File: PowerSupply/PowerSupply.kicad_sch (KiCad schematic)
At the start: 9 parts, among them J1 POWER, J2 CONTROL, J3 LASER, U0 AL8861Y-13

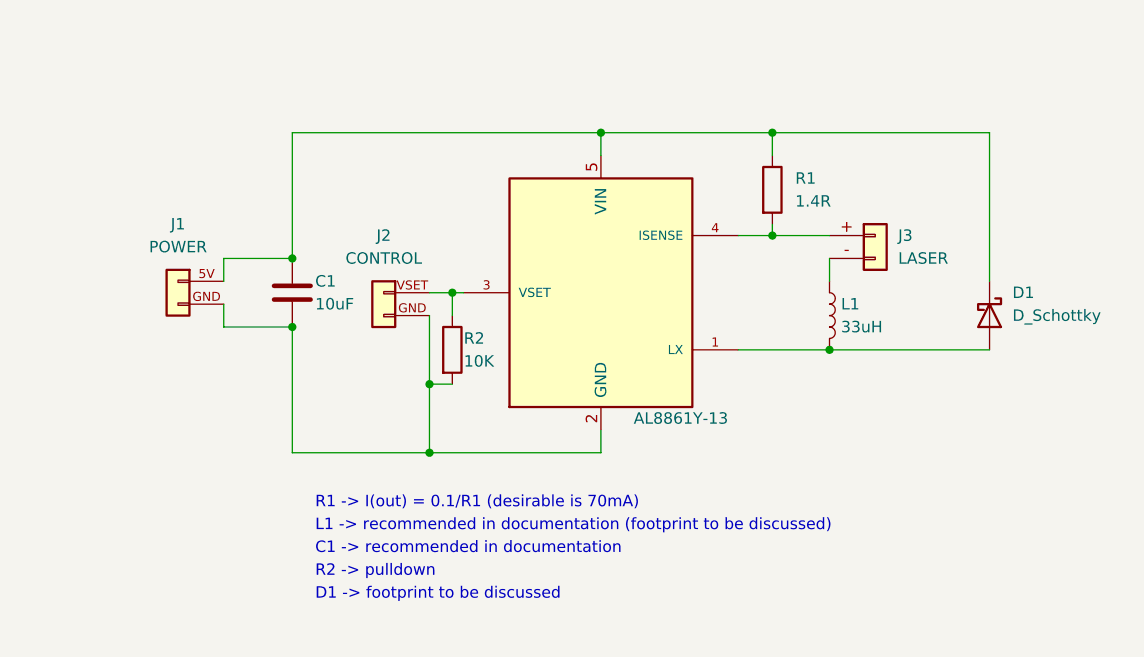
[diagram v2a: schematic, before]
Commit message: Add footprints
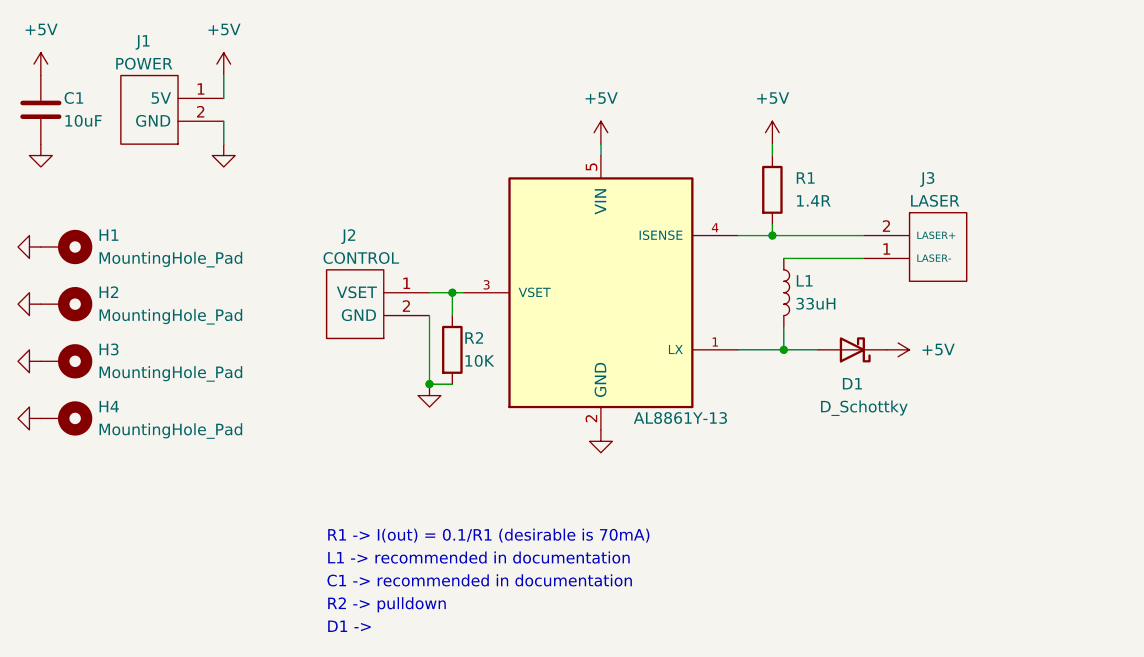
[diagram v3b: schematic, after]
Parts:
- removed J1: POWER, Connector_PinHeader_2.54mm:PinHeader_1x02_P2.54mm_Vertical, symbol Connector_Generic:Conn_01x02
- removed J2: CONTROL, Connector_PinHeader_2.54mm:PinHeader_1x02_P2.54mm_Vertical, symbol Connector_Generic:Conn_01x02
- removed J3: LASER, Connector_PinHeader_2.54mm:PinHeader_1x02_P2.54mm_Vertical, symbol Connector_Generic:Conn_01x02
- added H1, H2, H3, H4: MountingHole_Pad, MountingHole:MountingHole_3.2mm_M3_Pad, symbol Mechanical:MountingHole_Pad
- added J1: POWER, Connector_Molex:Molex_Nano-Fit_105313-xx02_1x02_P2.50mm_Horizontal, symbol Mouser:105313-1102
- added J2: CONTROL, Connector_Molex:Molex_Nano-Fit_105313-xx02_1x02_P2.50mm_Horizontal, symbol Mouser:105313-1102
- added J3: LASER, Connector_Molex:Molex_Nano-Fit_105313-xx02_1x02_P2.50mm_Horizontal, symbol Mouser:105313-1102
- C1: Height (none) -> 1.6; Manufacturer_Name (none) -> Kyocera AVX; Manufacturer_Part_Number (none) -> NOSA106M006R0800; Mouser Part Number (none) -> 581-NOSA106M006R0800; Mouser Price/Stock (none) -> https://cz.mouser.com/ProductDetail/Kyocera-AVX/NOSA106M006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
- D1: footprint Diode_SMD:D_1206_3216Metric_Pad1.42x1.75mm_HandSolder -> Diode_SMD:D_SOD-123F; Manufacturer_Name (none) -> Vishay; Manufacturer_Part_Number (none) -> SL02-GS08; Mouser Part Number (none) -> 78-SL02; Mouser Price/Stock (none) -> https://cz.mouser.com/ProductDetail/Vishay-Semiconductors/S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
- L1: footprint Inductor_SMD:L_1206_3216Metric_Pad1.42x1.75mm_HandSolder -> Custom:4800S; Height (none) -> 6; Manufacturer_Name (none) -> Murata; Manufacturer_Part_Number (none) -> 48330SC; Mouser Part Number (none) -> 580-48330SC; Mouser Price/Stock (none) -> https://cz.mouser.com/ProductDetail/Murata-Power-Solutions/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
- R1: Height (none) -> 0.5; Manufacturer_Name (none) -> Vishay; Manufacturer_Part_Number (none) -> CRCW12061R40FKEAHP; Mouser Part Number (none) -> 71-CRCW12061R40FKEAH; Mouser Price/Stock (none) -> https://cz.mouser.com/ProductDetail/Vishay-Dale/CRCW12061R4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
- R2: Height (none) -> 0.64; Manufacturer_Name (none) -> Vishay; Manufacturer_Part_Number (none) -> CRMA1206AF10M0DKEF; Mouser Part Number (none) -> 71-CRMA1206AF10M0DKF; Mouser Price/Stock (none) -> https://cz.mouser.com/ProductDetail/Vishay/CRMA1206AF10M0DK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
- U0: MANUFACTURER DIODES INCORPORATED -> (none); Manufacturer_Name (none) -> Diodes Incorporated; PARTREV 3-2 -> (none); STANDARD Manufacturer Recommendations -> (none)
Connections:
- net at R1.2, U0.4 (ISENSE): now also J3.2 (LASER+)
- net at L1.1: now also J3.1 (LASER-)
- net +5V: now reaches C1.1, D1.1 (K), R1.1, U0.5 (VIN)
- net +5V: now also J1.1 (5V)
- net GND: now reaches C1.2, R2.2, U0.2 (GND)
- net GND: now also H1.1, H2.1, H3.1, H4.1, J1.2 (GND), J2.2 (GND)
- net at R2.1, U0.3 (VSET): now also J2.1 (VSET)
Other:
- note added: "D1 ->"
- note added: "L1 -> recommended in documentation"
- note removed: "D1 -> footprint to be discussed"
- note removed: "L1 -> recommended in documentation (footprint to be discussed)"
- moved on the sheet: L1

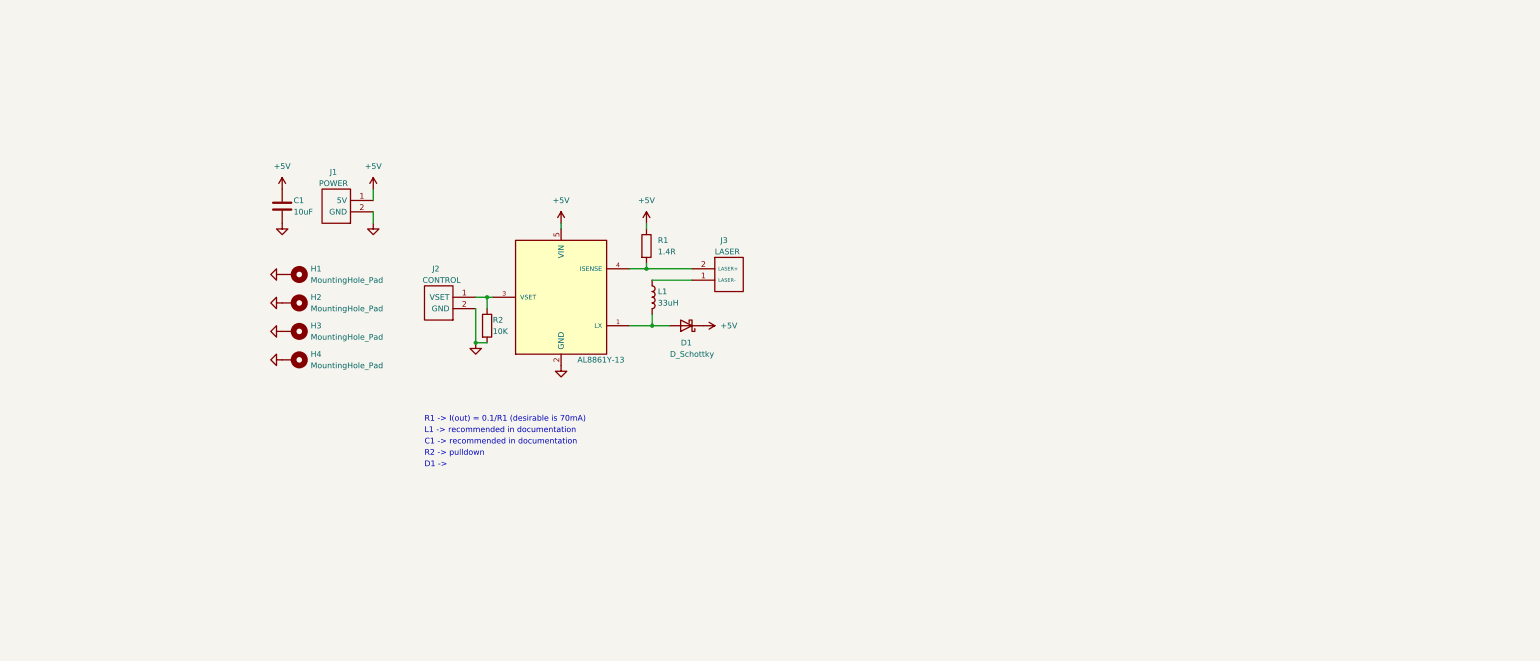
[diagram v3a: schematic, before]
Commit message: Review: 1st round - Schema & PCB - General modifications
All comments in design files, more on chat
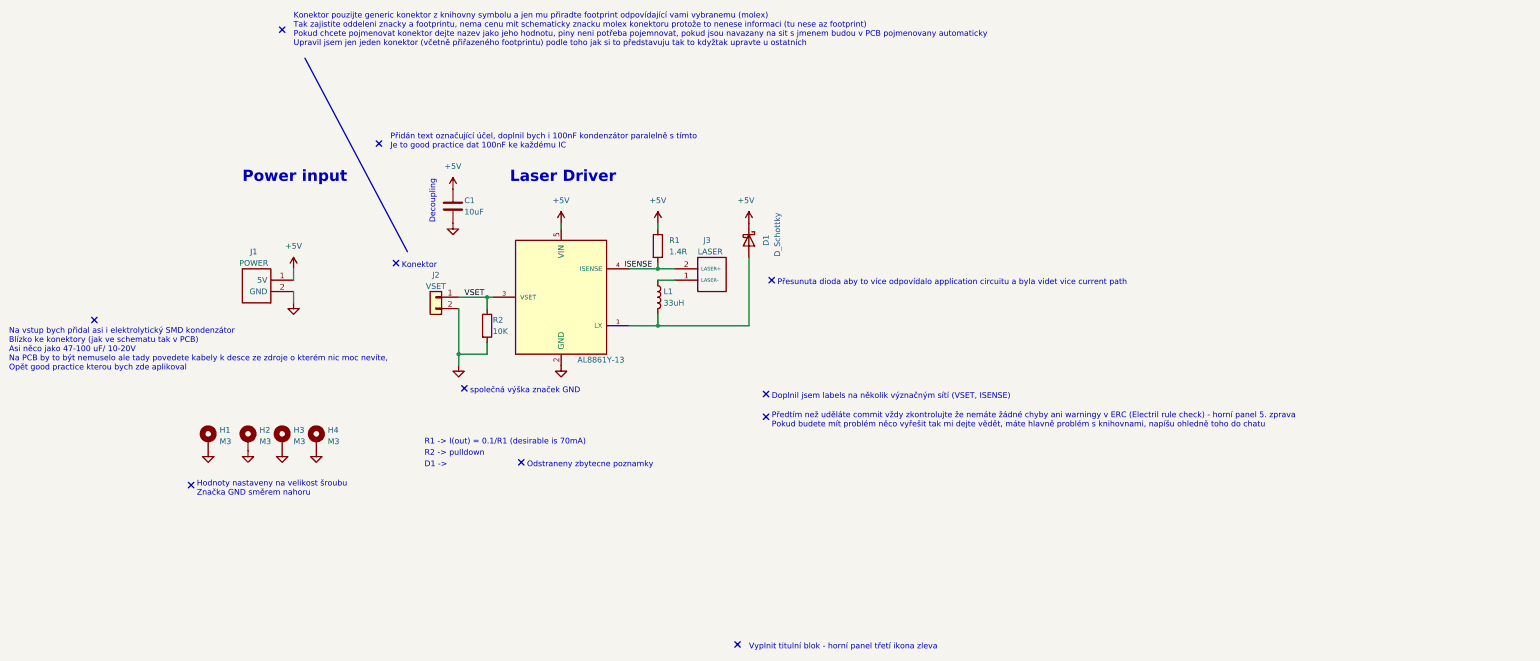
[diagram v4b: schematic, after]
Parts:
- removed J2: CONTROL, Connector_Molex:Molex_Nano-Fit_105313-xx02_1x02_P2.50mm_Horizontal, symbol Mouser:105313-1102
- added J2: VSET, Connector_Molex:Molex_Nano-Fit_105313-xx02_1x02_P2.50mm_Horizontal, symbol Connector_Generic:Conn_01x02
- H1, H2, H3, H4: value MountingHole_Pad -> M3; footprint MountingHole:MountingHole_3.2mm_M3_Pad -> MountingHole:MountingHole_3.2mm_M3_Pad_Via
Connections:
- net GND: now also J2.2 (Pin_2)
- net ISENSE: now reaches J3.2 (LASER+), R1.2, U0.4 (ISENSE)
- net VSET: now reaches R2.1, U0.3 (VSET)
- net VSET: now also J2.1 (Pin_1)
- no-connect marks 0 -> 11
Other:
- note added: "Decoupling"
- note added: "Doplnil jsem labels na několik význačným sítí (VSET, ISENSE)"
- note added: "Hodnoty nastaveny na velikost šroubu Značka GND směrem nahoru"
- note added: "Konektor"
- note added: "Konektor pouzijte generic konektor z knihovny symbolu a jen mu přiradte footprint odpovídající vami vybranemu (molex) Tak zajistite oddeleni znacky a footprintu, nema cenu mit schematicky znacku molex konektoru protože to nenese informaci (tu nese az footprint) Pokud chcete pojmenovat konektor dejte nazev jako jeho hodnotu, piny neni potřeba pojemnovat, pokud jsou navazany na sit s jmenem budou v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"
- note added: "Laser Driver"
- note added: "Na vstup bych přidal asi i elektrolytický SMD kondenzátor Blízko ke konektory (jak ve schematu tak v PCB) Asi něco jako 47-100 uF/ 10-20V Na PCB by to být nemuselo ale tady povedete kabely k desce ze zdroje o kterém nic moc nevíte, Opět good practice kterou bych zde aplikoval"
- note added: "Odstraneny zbytecne poznamky"
- note added: "Power input"
- note added: "Předtím než uděláte commit vždy zkontrolujte že nemáte žádné chyby ani warningy v ERC (Electril rule check) - horní panel 5. zprava Pokud budete mít problém něco vyřešit tak mi dejte vědět, máte hlavně problém s knihovnami, napíšu ohledně toho do chatu"
- note added: "Přesunuta dioda aby to více odpovídalo application circuitu a byla videt vice current path"
- note added: "Přidán text označující účel, doplnil bych i 100nF kondenzátor paralelně s tímto Je to good practice dat 100nF ke každému IC"
- note added: "Vyplnit titulní blok - horní panel třetí ikona zleva"
- note added: "společná výška značek GND"
- note removed: "C1 -> recommended in documentation"
- note removed: "L1 -> recommended in documentation"
- moved on the sheet: C1, D1, H1, H2, H3, H4, J1, J3, L1, R1

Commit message: Resolved first review, Routing
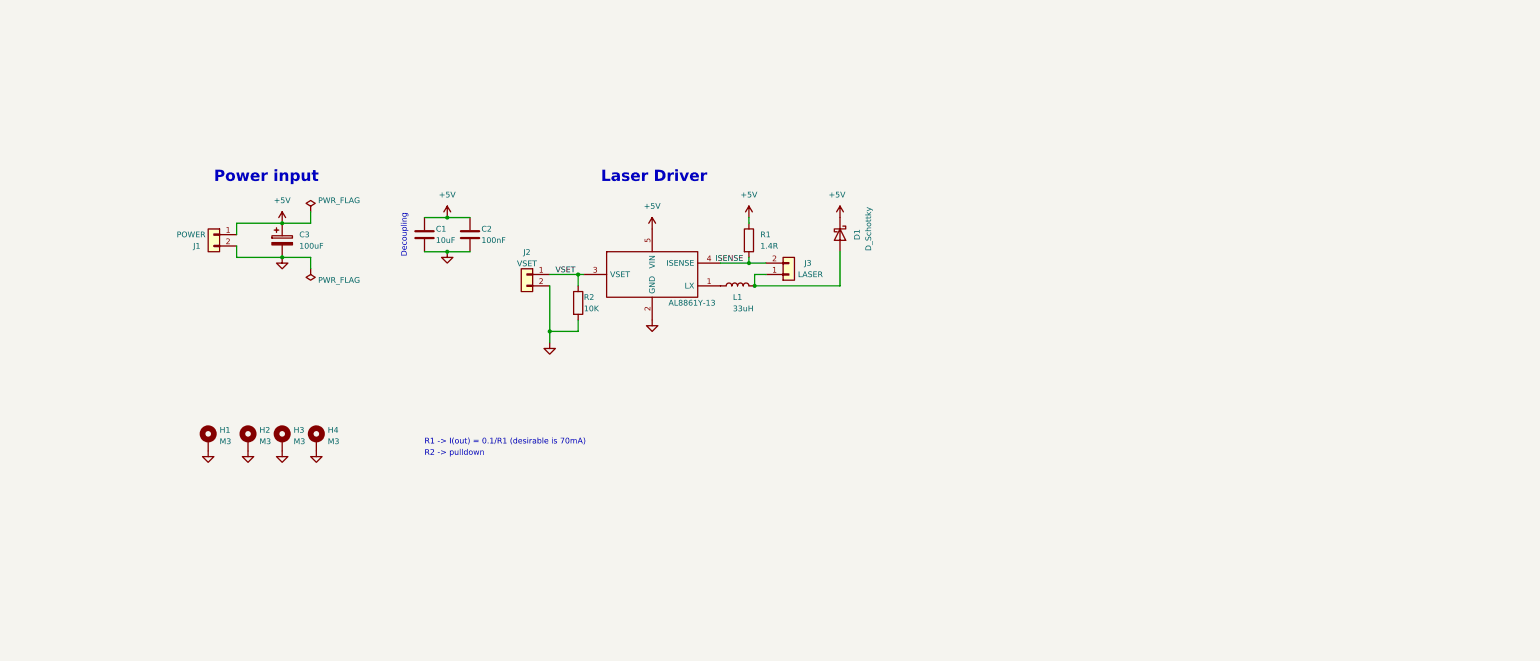
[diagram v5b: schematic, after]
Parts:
- removed J1: POWER, Connector_Molex:Molex_Nano-Fit_105313-xx02_1x02_P2.50mm_Horizontal, symbol Mouser:105313-1102
- removed J3: LASER, Connector_Molex:Molex_Nano-Fit_105313-xx02_1x02_P2.50mm_Horizontal, symbol Mouser:105313-1102
- added C2: 100nF, Capacitor_SMD:C_1206_3216Metric_Pad1.33x1.80mm_HandSolder, symbol Device:C
- added C3: 100uF, Capacitor_SMD:CP_Elec_5x5.3, symbol Device:C_Polarized
- added J1: POWER, Connector_Molex:Molex_Nano-Fit_105313-xx02_1x02_P2.50mm_Horizontal, symbol Connector_Generic:Conn_01x02
- added J3: LASER, Connector_Molex:Molex_Nano-Fit_105313-xx02_1x02_P2.50mm_Horizontal, symbol Connector_Generic:Conn_01x02
- U0: footprint Package_TO_SOT_SMD:SOT-89-5 -> SOT89-5; Manufacturer_Name Diodes Incorporated -> Diodes Inc.; Manufacturer_Part_Number (none) -> AL8861Y-13; Mouser Part Number (none) -> 621-AL8861Y-13; Mouser Price/Stock (none) -> https://www.mouser.co.uk/ProductDetail/Diodes-Incorporated/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
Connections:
- net +5V: now also C2.1, C3.1, J1.1 (Pin_1)
- net GND: now also C2.2, C3.2, J1.2 (Pin_2)
- net ISENSE: now also J3.2 (Pin_2)
- net at D1.2 (A), L1.2: now also J3.1 (Pin_1); no longer U0.1 (LX)
- net at L1.1: now also U0.1 (LX)
- no-connect marks 11 -> 0
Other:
- note removed: "D1 ->"
- note removed: "Doplnil jsem labels na několik význačným sítí (VSET, ISENSE)"
- note removed: "Hodnoty nastaveny na velikost šroubu Značka GND směrem nahoru"
- note removed: "Konektor"
- note removed: "Konektor pouzijte generic konektor z knihovny symbolu a jen mu přiradte footprint odpovídající vami vybranemu (molex) Tak zajistite oddeleni znacky a footprintu, nema cenu mit schematicky znacku molex konektoru protože to nenese informaci (tu nese az footprint) Pokud chcete pojmenovat konektor dejte nazev jako jeho hodnotu, piny neni potřeba pojemnovat, pokud jsou navazany na sit s jmenem budou v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"
- note removed: "Na vstup bych přidal asi i elektrolytický SMD kondenzátor Blízko ke konektory (jak ve schematu tak v PCB) Asi něco jako 47-100 uF/ 10-20V Na PCB by to být nemuselo ale tady povedete kabely k desce ze zdroje o kterém nic moc nevíte, Opět good practice kterou bych zde aplikoval"
- note removed: "Odstraneny zbytecne poznamky"
- note removed: "Předtím než uděláte commit vždy zkontrolujte že nemáte žádné chyby ani warningy v ERC (Electril rule check) - horní panel 5. zprava Pokud budete mít problém něco vyřešit tak mi dejte vědět, máte hlavně problém s knihovnami, napíšu ohledně toho do chatu"
- note removed: "Přesunuta dioda aby to více odpovídalo application circuitu a byla videt vice current path"
- note removed: "Přidán text označující účel, doplnil bych i 100nF kondenzátor paralelně s tímto Je to good practice dat 100nF ke každému IC"
- note removed: "Vyplnit titulní blok - horní panel třetí ikona zleva"
- note removed: "společná výška značek GND"
- company: (none) -> Adam Procházka VUT FIT 
- title: (none) -> Laser Driver
- moved on the sheet: C1, D1, J2, L1, R1, R2
